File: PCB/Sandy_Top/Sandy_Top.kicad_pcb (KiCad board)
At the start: 2 copper layers, 285 x 37 mm, 64 parts, among them J1 Conn_02x02_Top_Bottom, J2 Conn_02x02_Top_Bottom, J3 Conn_02x02_Top_Bottom

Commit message: 組み立ての目安となるシルク追加
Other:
- board text added: "Back Side"
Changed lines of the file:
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@@
     (fp_arc (start -140.510786 -0.814254) (mid -141.925 -1.40004) (end -142.510786 -2.814254) (layer "Edge.Cuts") (width 0.3))
     (fp_arc (start -39.470786 -0.82504) (mid -38.056572 -0.239254) (end -37.470786 1.17496) (layer "Edge.Cuts") (width 0.3))
-    (fp_arc (start 142.475 -2.814254) (mid 141.889203 -1.400035) (end 140.475 -0.814254) (layer "Edge.Cuts") (width 0.3))
+    (fp_arc (start 142.475 -2.814254) (mid 141.889197 -1.40007) (end 140.475 -0.814254) (layer "Edge.Cuts") (width 0.3))
     (fp_arc (start -35.470786 18.24996) (mid -36.885 17.664174) (end -37.470786 16.24996) (layer "Edge.Cuts") (width 0.3))
-    (fp_arc (start 140.475 -18.75004) (mid 141.889257 -18.164285) (end 142.475 -16.75004) (layer "Edge.Cuts") (width 0.3))
+    (fp_arc (start 140.475 -18.75004) (mid 141.889222 -18.164279) (end 142.475 -16.75004) (layer "Edge.Cuts") (width 0.3))
     (fp_arc (start -142.525 -16.75004) (mid -141.939214 -18.164254) (end -140.525 -18.75004) (layer "Edge.Cuts") (width 0.3))
     (fp_circle (center -47.625 -14.50004) (end -45.425 -14.50004) (layer "Edge.Cuts") (width 0.15) (fill none))
@@
     (effects (font (size 1.5 1.5) (thickness 0.3)) (justify mirror))
   )
+  (gr_text "Back Side" (at 183.76131 36.528405) (layer "B.SilkS")
+    (effects (font (size 2.5 2.5) (thickness 0.3) italic) (justify mirror))
+  )
   (gr_text "#Sandy_kbd v.0.1, Top\nby @jpskenn" (at 173.458435 50.815905) (layer "B.SilkS")

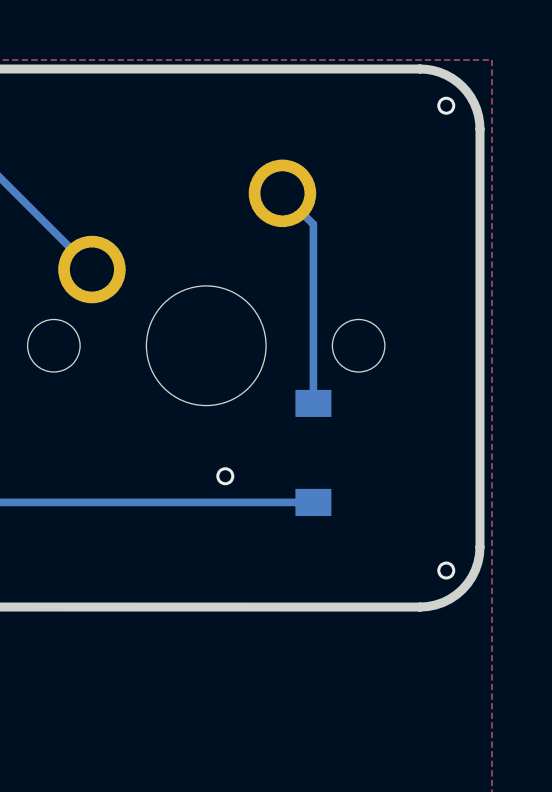
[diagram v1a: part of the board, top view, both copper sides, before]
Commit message: ダイオードの方向を強調するシルクに変更
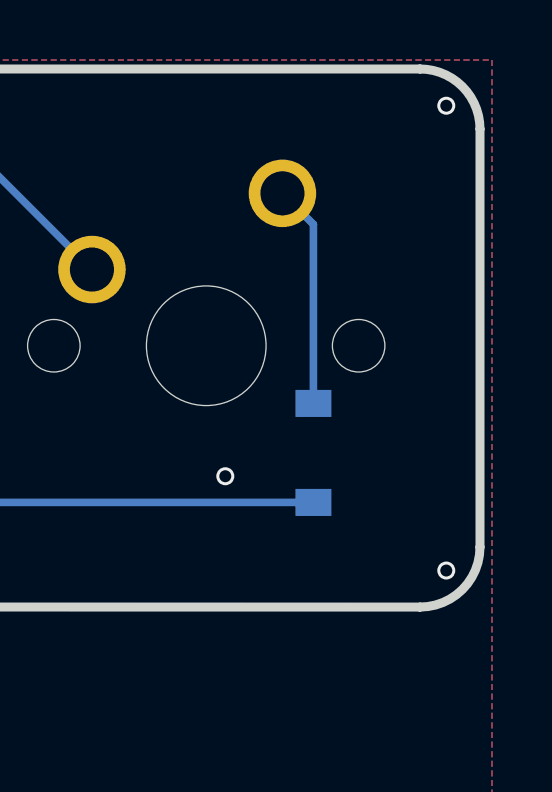
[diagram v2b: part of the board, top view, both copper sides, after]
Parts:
- D1, D10, D11, D12, D13, D14, D15, D16, D17, D18, D19, D2, D3, D4, D5, D6, D7, D8, D9: footprint Diode_SMD:D_SOD-123 -> locallib:D_SOD-123_Emphasized_Direction_Line
